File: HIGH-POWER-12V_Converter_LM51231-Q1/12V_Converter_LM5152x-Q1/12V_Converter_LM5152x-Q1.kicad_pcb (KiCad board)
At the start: 2 copper layers, 47.2 x 39.6 mm, 34 parts, among them M1 60V, M2 60V, U1 LM51521QRGRRQ1

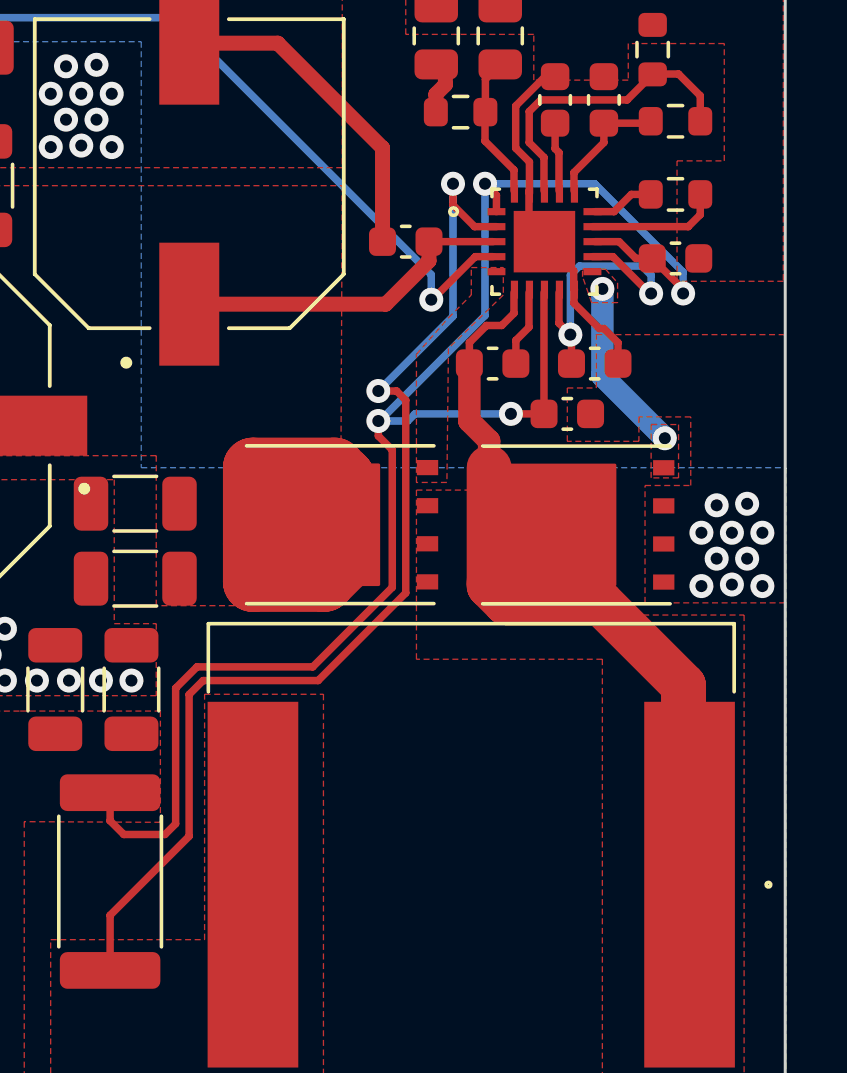
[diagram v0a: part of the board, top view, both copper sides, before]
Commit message: updated mosfets on high power 12V
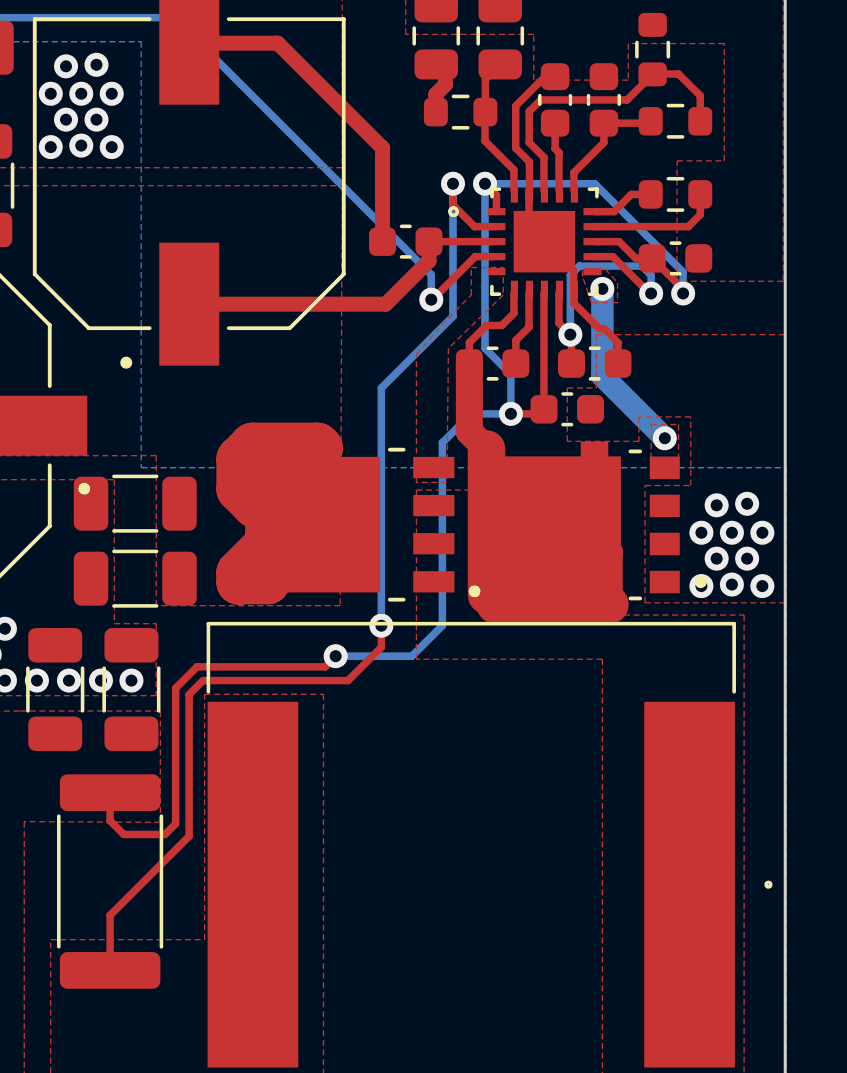
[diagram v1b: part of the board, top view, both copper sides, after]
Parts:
- M1: footprint n-MOS:SIR826ADP-T1-GE3 -> M1:TRANS_NVMFS5834NLWFT1G
- M2: value 60V -> CSD18540Q5B; footprint n-MOS:SIR826ADP-T1-GE3 -> M2:TRANS_CSD18540Q5B
- moved M2 0.35 mm to (94.5, 108.9)
- moved M1 0.20 mm to (102.2, 108.9)
- moved Cbias1 0.15 mm to (101.7, 105.1)
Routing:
- net Net-(Cbst1-Pad2): track 25.0 -> 18.5 mm
- net Vout: track 46.7 -> 42.6 mm
- net Vin: track 54.8 -> 53.0 mm
- net Net-(L1-Pad2): track 36.8 -> 36.2 mm

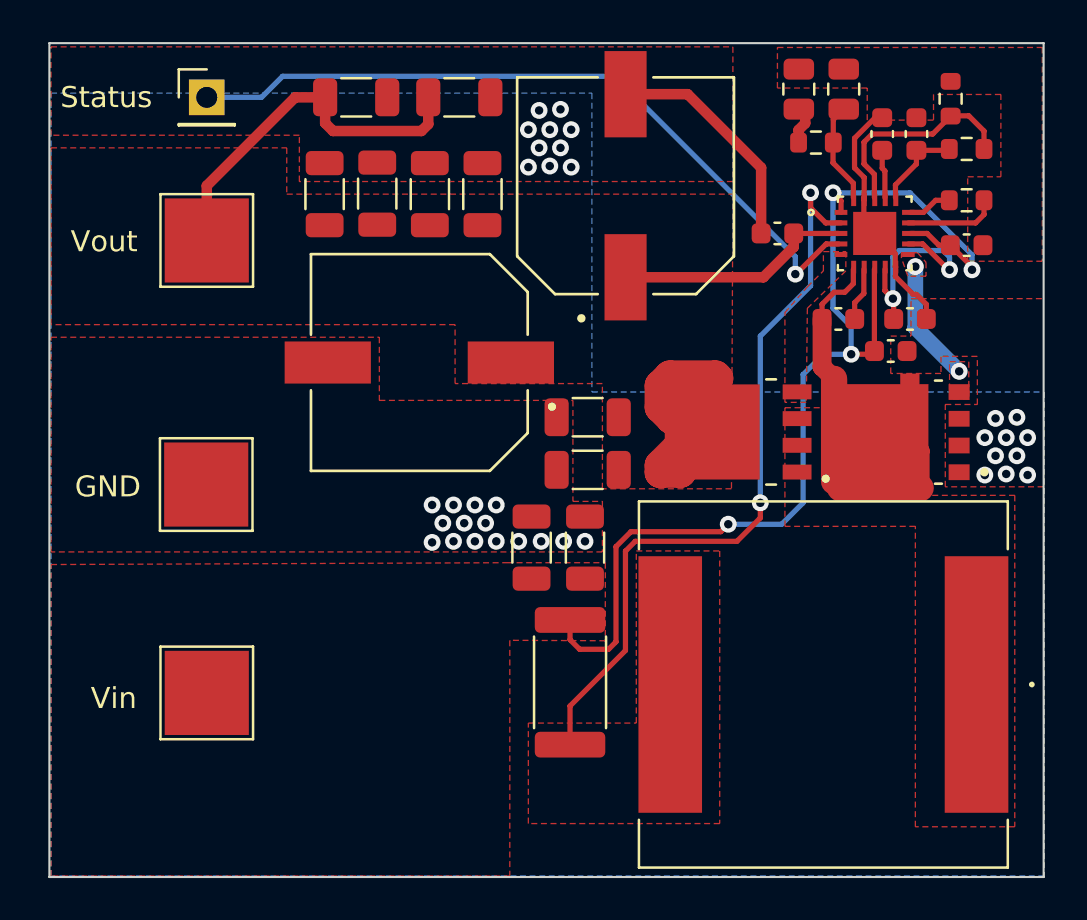
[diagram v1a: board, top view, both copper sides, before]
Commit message: updated high power to reflect changes described in review notes
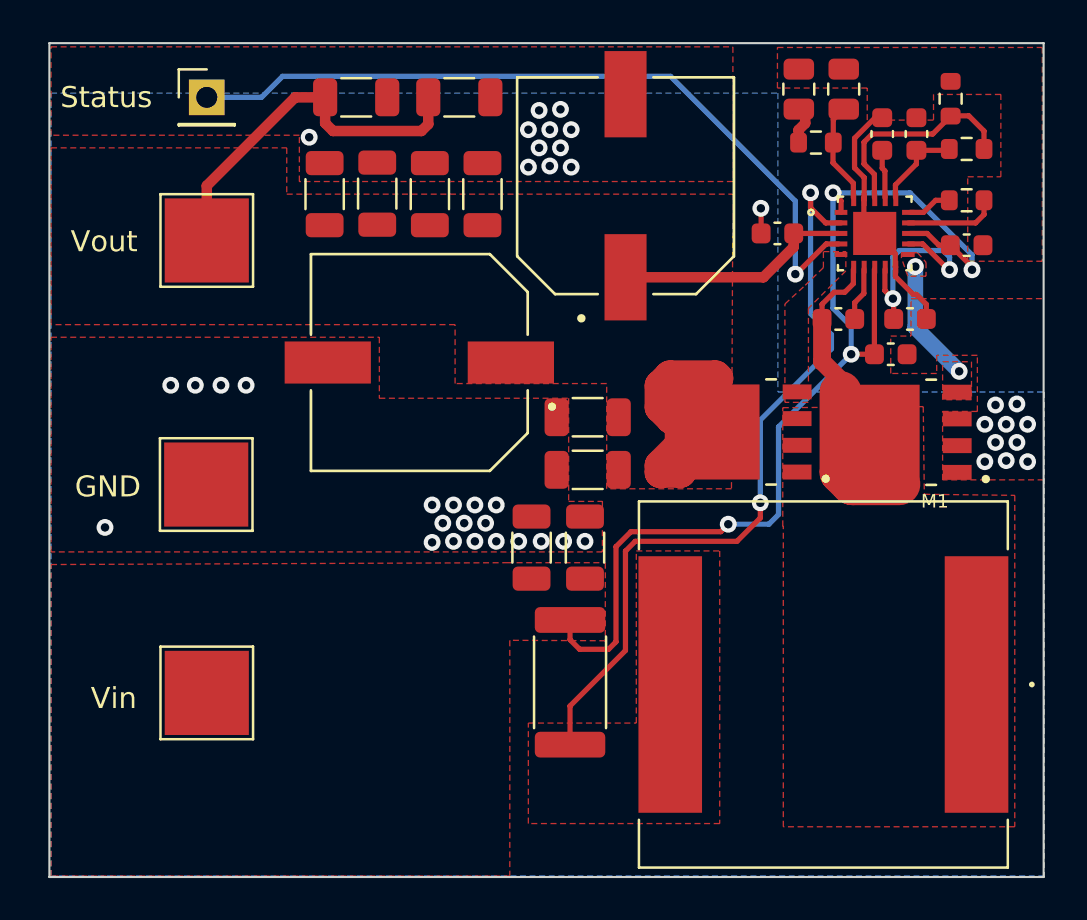
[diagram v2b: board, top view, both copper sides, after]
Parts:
- L1: value 2.2 -> 2.2u
- M1: value 60V -> CSD18540Q5B; footprint M1:TRANS_NVMFS5834NLWFT1G -> M2:TRANS_CSD18540Q5B
- moved Cbias1 0.15 mm to (101.7, 105.2)
- moved M1 0.11 mm to (102.1, 108.9)
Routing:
- net GND: track 27.3 -> 17.4 mm, vias 35 -> 42
- net Net-(Cbst1-Pad2): track 18.5 -> 14.0 mm
- net status: track 35.4 -> 37.0 mm
- net Vin: track 53.0 -> 51.9 mm
- net Net-(L1-Pad2): track 36.2 -> 37.1 mm
